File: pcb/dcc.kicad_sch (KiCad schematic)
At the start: 69 parts, among them U10 LM339, U11 LM339, U4 L78L05_SOT89, U5 L79L05_SOT89, U6 LM339, U7 LM339, U8 LM339, U9 4052

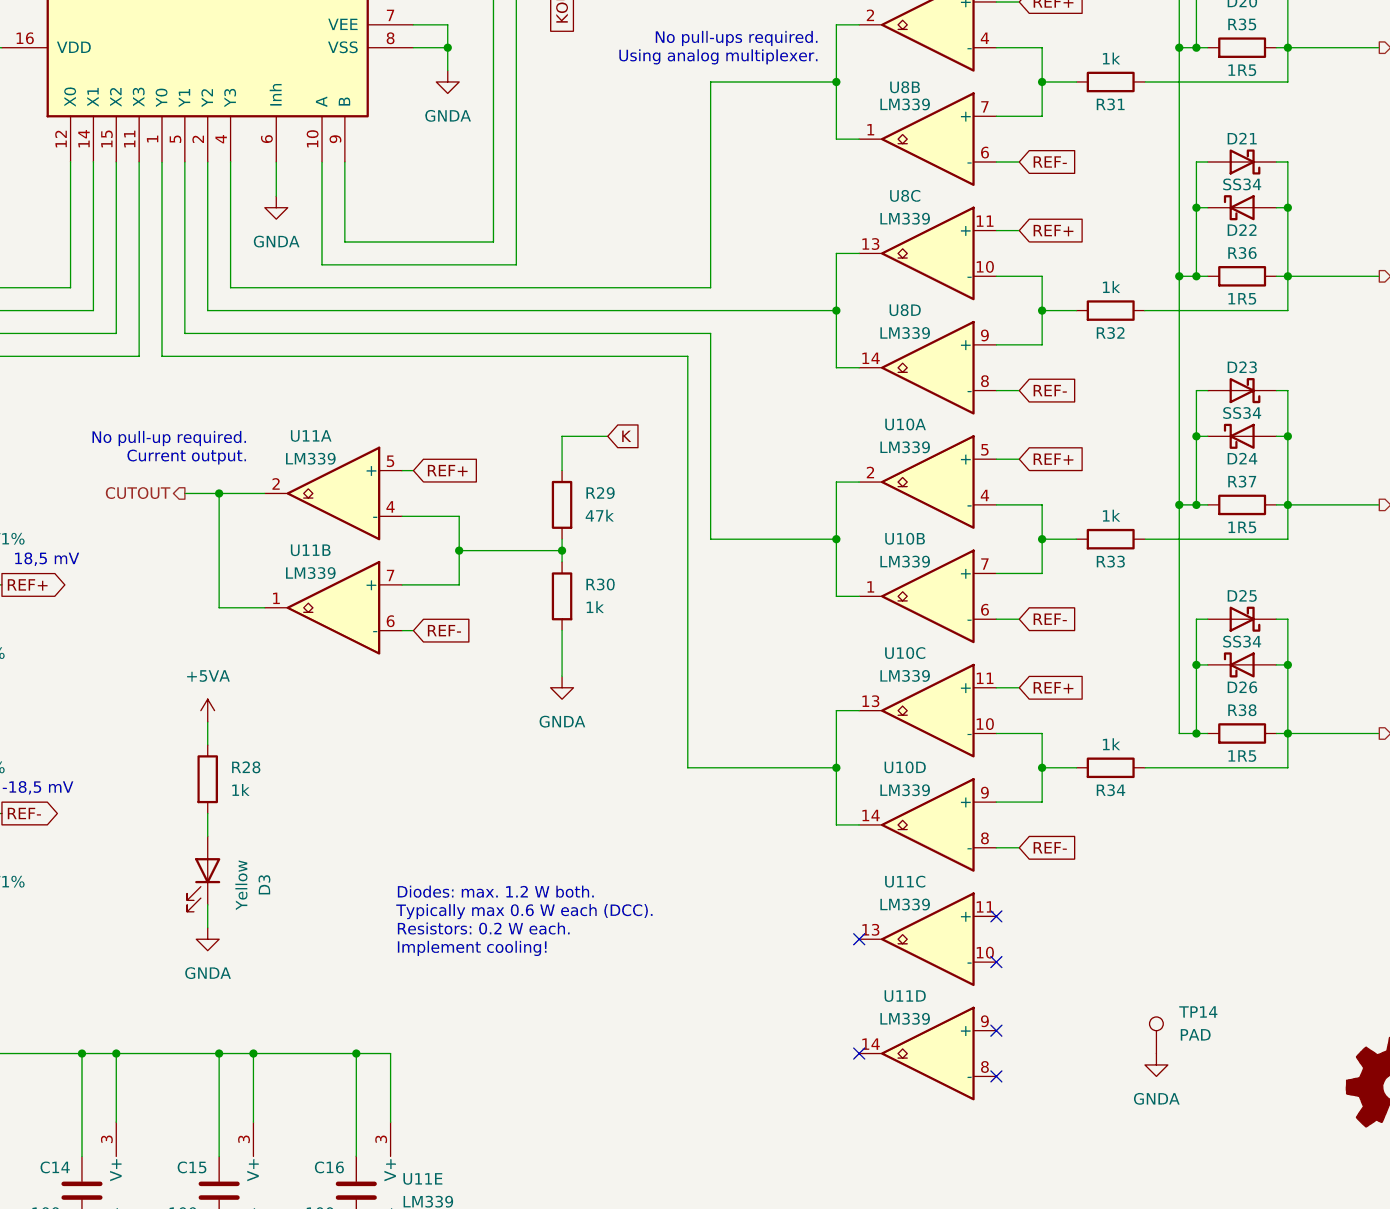
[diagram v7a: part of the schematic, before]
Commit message: pcb: wire multiplexer's inputs.
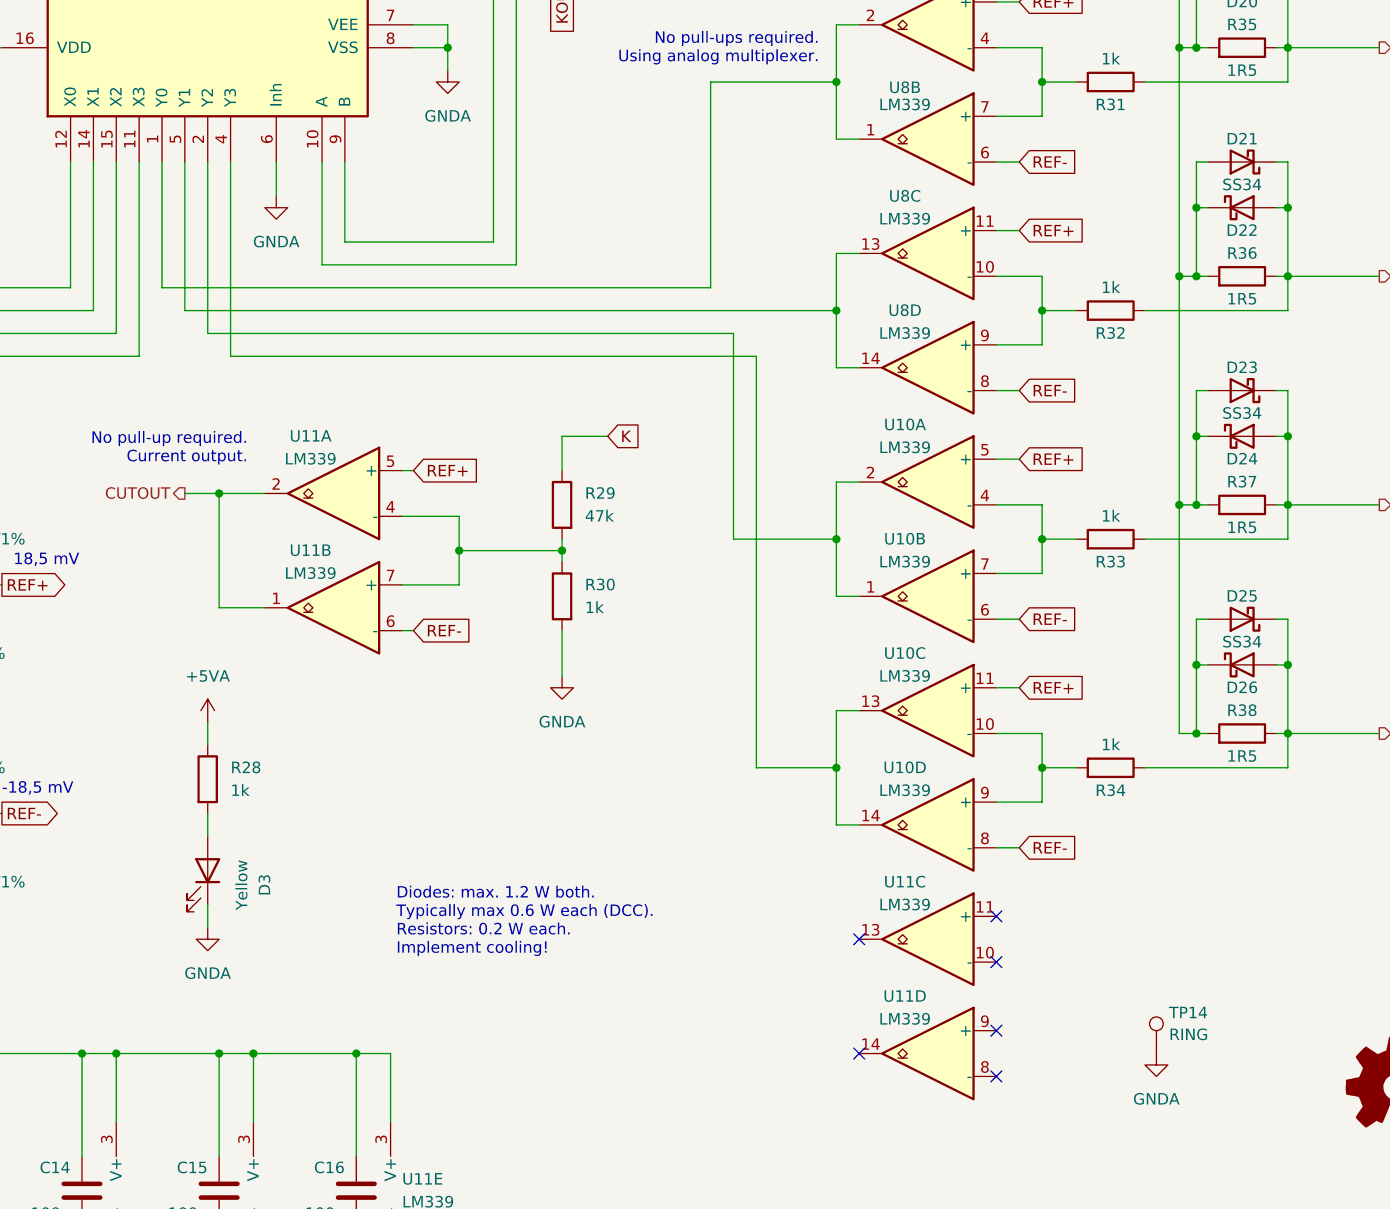
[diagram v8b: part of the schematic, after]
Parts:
- TP14: value PAD -> RING; footprint TestPoint:TestPoint_Pad_D2.0mm -> TestPoint:TestPoint_Loop_D1.80mm_Drill1.0mm_Beaded
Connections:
- net at U10.1, U10.2: now also U9.2 (Y2); no longer U9.5 (Y1)
- net at U8.13, U8.14: now also U9.5 (Y1); no longer U9.2 (Y2)
- net at U8.1, U8.2: now also U9.1 (Y0); no longer U9.4 (Y3)
- net at U10.13, U10.14: now also U9.4 (Y3); no longer U9.1 (Y0)
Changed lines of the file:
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@@
-    (stroke (width 0) (type default))
-  )
-  (wire (pts (xy 143.51 72.39) (xy 143.51 55.88))
     (stroke (width 0) (type default))
   )
@@
     (stroke (width 0) (type default))
   )
-  (wire (pts (xy 199.39 74.93) (xy 199.39 97.79))
+  (wire (pts (xy 201.93 74.93) (xy 201.93 97.79))
     (stroke (width 0) (type default))
   )
@@
     (stroke (width 0) (type default))
   )
-  (wire (pts (xy 138.43 77.47) (xy 196.85 77.47))
+  (wire (pts (xy 146.05 77.47) (xy 204.47 77.47))
     (stroke (width 0) (type default))
   )
@@
     (stroke (width 0) (type default))
   )
-  (wire (pts (xy 199.39 97.79) (xy 213.36 97.79))
+  (wire (pts (xy 201.93 97.79) (xy 213.36 97.79))
     (stroke (width 0) (type default))
   )
@@
     (stroke (width 0) (type default))
   )
-  (wire (pts (xy 196.85 123.19) (xy 213.36 123.19))
+  (wire (pts (xy 204.47 123.19) (xy 213.36 123.19))
     (stroke (width 0) (type default))
   )
@@
     (stroke (width 0) (type default))
   )
-  (wire (pts (xy 140.97 74.93) (xy 140.97 55.88))
-    (stroke (width 0) (type default))
-  )
   (wire (pts (xy 133.35 185.42) (xy 129.54 185.42))
     (stroke (width 0) (type default))
@@
     (stroke (width 0) (type default))
   )
-  (wire (pts (xy 199.39 69.85) (xy 146.05 69.85))
+  (wire (pts (xy 138.43 69.85) (xy 199.39 69.85))
     (stroke (width 0) (type default))
   )
@@
     (stroke (width 0) (type default))
   )
+  (wire (pts (xy 138.43 55.88) (xy 138.43 69.85))
+    (stroke (width 0) (type default))
+  )
   (wire (pts (xy 58.42 170.18) (xy 58.42 172.72))
     (stroke (width 0) (type default))
@@
     (stroke (width 0) (type default))
   )
+  (wire (pts (xy 143.51 55.88) (xy 143.51 74.93))
+    (stroke (width 0) (type default))
+  )
   (wire (pts (xy 25.4 151.13) (xy 25.4 154.94))
     (stroke (width 0) (type default))
@@
     (stroke (width 0) (type default))
   )
+  (wire (pts (xy 140.97 55.88) (xy 140.97 72.39))
+    (stroke (width 0) (type default))
+  )
   (wire (pts (xy 175.26 27.94) (xy 175.26 64.77))
     (stroke (width 0) (type default))
@@
     (stroke (width 0) (type default))
   )
-  (wire (pts (xy 196.85 77.47) (xy 196.85 123.19))
+  (wire (pts (xy 204.47 77.47) (xy 204.47 123.19))
     (stroke (width 0) (type default))
   )
@@
     (stroke (width 0) (type default))
   )
-  (wire (pts (xy 138.43 77.47) (xy 138.43 55.88))
-    (stroke (width 0) (type default))
-  )
   (wire (pts (xy 36.83 185.42) (xy 40.64 185.42))
     (stroke (width 0) (type default))
@@
     (stroke (width 0) (type default))
   )
-  (wire (pts (xy 146.05 69.85) (xy 146.05 55.88))
-    (stroke (width 0) (type default))
-  )
   (wire (pts (xy 163.83 177.8) (xy 163.83 185.42))
     (stroke (width 0) (type default))
@@
     (stroke (width 0) (type default))
   )
+  (wire (pts (xy 146.05 55.88) (xy 146.05 77.47))
+    (stroke (width 0) (type default))
+  )
   (wire (pts (xy 166.37 90.17) (xy 165.1 90.17))
     (stroke (width 0) (type default))
@@
     (stroke (width 0) (type default))
   )
-  (wire (pts (xy 143.51 72.39) (xy 213.36 72.39))
+  (wire (pts (xy 140.97 72.39) (xy 213.36 72.39))
     (stroke (width 0) (type default))
   )
@@
     (stroke (width 0) (type default))
   )
-  (wire (pts (xy 140.97 74.93) (xy 199.39 74.93))
+  (wire (pts (xy 143.51 74.93) (xy 201.93 74.93))
     (stroke (width 0) (type default))
   )
@@
   (symbol (lib_id "Connector:TestPoint") (at 248.92 154.94 0) (unit 1)
     (in_bom yes) (on_board yes) (dnp no) (fields_autoplaced)
-    (property "Reference" "TP14" (at 251.46 150.368 0)
+    (property "Reference" "TP14" (at 250.317 150.4259 0)
       (effects (font (size 1.27 1.27)) (justify left))
     )
-    (property "Value" "PAD" (at 251.46 152.908 0)
+    (property "Value" "RING" (at 250.317 152.8501 0)
       (effects (font (size 1.27 1.27)) (justify left))
     )
-    (property "Footprint" "TestPoint:TestPoint_Pad_D2.0mm" (at 254 154.94 0)
-      (effects (font (size 1.27 1.27)) hide)
-    )
+    (property "Footprint" "TestPoint:TestPoint_Loop_D1.80mm_Drill1.0mm_Beaded" (at 254 154.94 0)
+      (effects (font (size 1.27 1.27)) hide)
+    )
